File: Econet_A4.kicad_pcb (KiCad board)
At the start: 4 copper layers, 121 x 59.6 mm, 57 parts, among them IC1 SP485REN-L, IC2 74LS123, IC3 LM319M, IC4 LM319M, IC5 68B54, IC6 74AHCT132, IC7 74HCT244, IC8 74HCT245, Q1 AO3401A

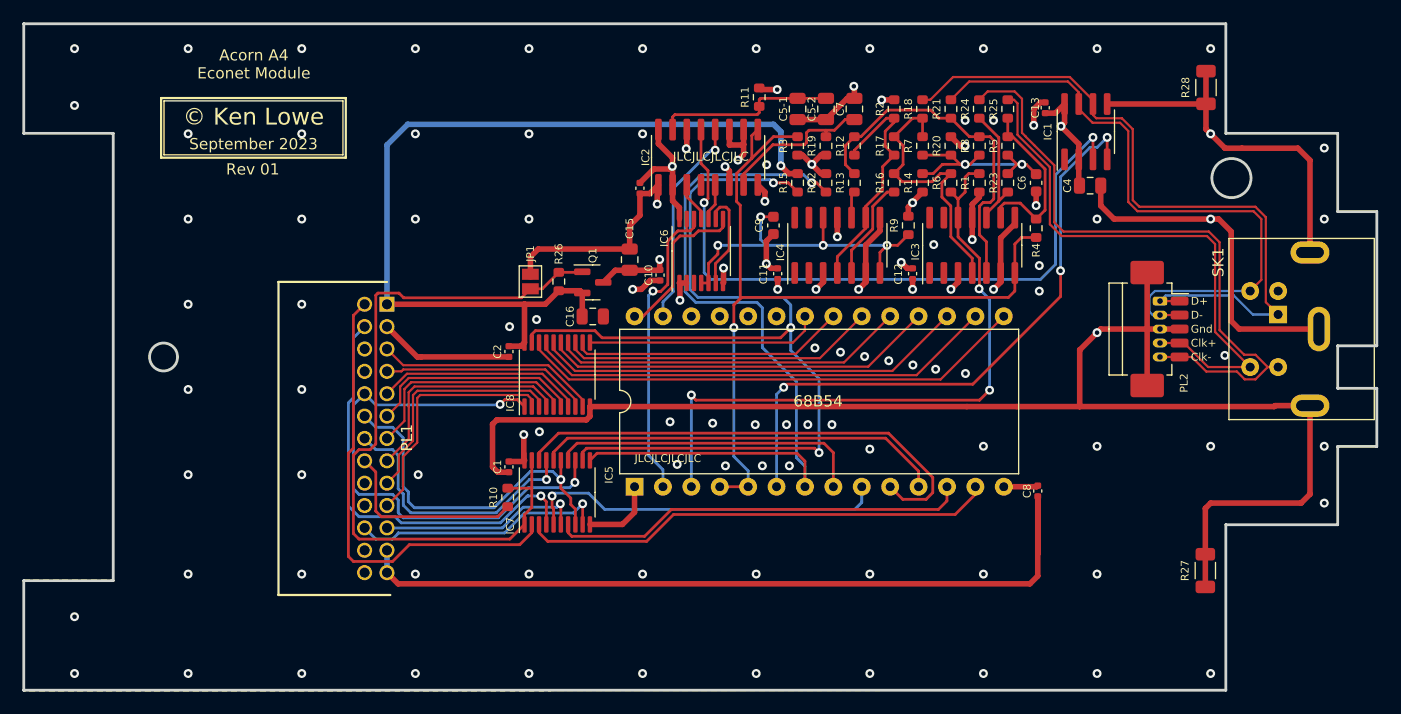
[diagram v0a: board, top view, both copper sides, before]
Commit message: Correct IC 8 data direction
Corrected IC8 data direction
Added activity LEDs
Changed IC7 from 244 to 245
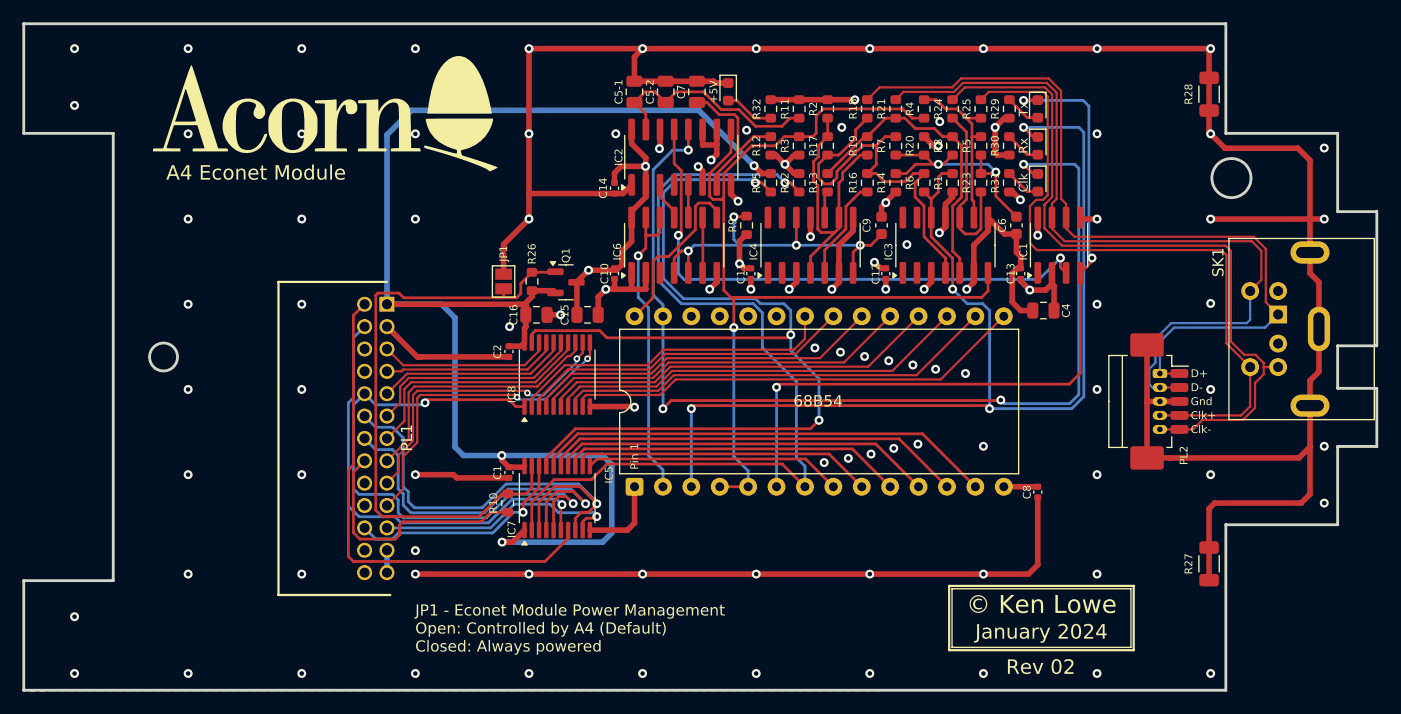
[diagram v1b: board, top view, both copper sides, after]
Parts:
- added G1: LOGO, Econet_A4:AcornLogo2, F.Cu at (132.4, 86.2)
- added LED1: Red, LED_SMD:LED_0603_1608Metric, F.Cu at (195.7, 85.6)
- added LED2: Green, LED_SMD:LED_0603_1608Metric, F.Cu at (195.7, 88.9)
- added LED3: Blue, LED_SMD:LED_0603_1608Metric, F.Cu at (195.7, 92.2)
- added LED4: Green, LED_SMD:LED_0603_1608Metric, F.Cu at (168.0, 84.0)
- added R29: 470R, Resistor_SMD:R_0603_1608Metric, F.Cu at (193.1, 85.6)
- added R30: 1K0, Resistor_SMD:R_0603_1608Metric, F.Cu at (193.1, 88.9)
- added R31: 220R, Resistor_SMD:R_0603_1608Metric, F.Cu at (193.1, 92.2)
- added R32: 2K2, Resistor_SMD:R_0603_1608Metric, F.Cu at (171.8, 85.6)
- IC6: footprint Package_SO:TSSOP-14_4.4x5mm_P0.65mm -> Package_SO:SOIC-14_3.9x8.7mm_P1.27mm
- IC7: value 74HCT244 -> 74HCT245
- PL2: value Conn_01x07 -> Conn_01x06
- SK1: footprint Econet_A4:Connector_Mini-DIN_Female_5Pin_2rows -> Econet_A4:Connector_Mini-DIN_Female_6Pin_2rows
- moved C13 15.0 mm to (194.1, 100.3)
- moved C5-1 14.7 mm to (159.6, 84.0), turned to 90 degrees
- moved R4 14.6 mm to (185.5, 85.6)
- moved R9 14.5 mm to (169.6, 96.0), turned to 90 degrees
- moved C5-2 14.4 mm to (162.4, 84.0), turned to 90 degrees
- moved C7 14.2 mm to (165.2, 84.0)
- moved C4 11.9 mm to (196.2, 103.6), turned to 180 degrees
- moved IC1 10.4 mm to (197.6, 97.8)
- moved C9 9.67 mm to (181.7, 96.0), turned to -90 degrees
- moved PL2 6.48 mm to (205.9, 111.7)
- moved C15 6.21 mm to (155.4, 104.0), turned to 0 degrees
- moved R17 5.95 mm to (176.9, 88.9), turned to 90 degrees
- moved R2 5.95 mm to (176.9, 85.6)
- moved C16 5.04 mm to (150.8, 104.0)
- moved R12 4.94 mm to (171.8, 88.9)
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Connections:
- net Net-(IC1-DI) renamed /Tx_Data
- net Net-(IC2B-~{Q}) renamed /Econet_Clk
- net Net-(IC5-Rx_Data) renamed /Rx_Data
- C5-1 pad 1: Net-(IC2A-RCext) -> GND
- C5-2 pad 1: Net-(IC2A-RCext) -> GND
- IC2 pad 15: Net-(IC2A-RCext) -> GND
- IC7 pad 1: /ECON -> +5V
- IC7 pad 11: /ADLC_nIRQ -> /ADLC_nRST
- IC7 pad 12: /IC8_nCE -> /ADLC_nCS
- IC7 pad 13: /A4_WBE -> /ADLC_A0
- IC7 pad 14: /ADLC_nRST -> /ADLC_A1
- IC7 pad 15: /A4_S2 -> /ADLC_RnW
- IC7 pad 16: /ADLC_A1 -> /ADLC_Clock
- IC7 pad 17: /A4_CLK2 -> /IC8_nCE
- IC7 pad 18: /ADLC_A0 -> /A4_EFIQ
- IC7 pad 2: /A4_LA2 -> /ADLC_nIRQ
- IC7 pad 3: /ADLC_Clock -> /A4_S2
- IC7 pad 4: /A4_LA3 -> /A4_CLK2
- IC7 pad 5: /ADLC_nCS -> /A4_WBE
- IC7 pad 6: /A4_nRST -> /A4_LA3
- IC7 pad 7: /ADLC_RnW -> /A4_LA2
- IC7 pad 9: /A4_EFIQ -> /A4_nRST
- IC8 pad 11: /ADLC_D0 -> /A4_D7
- IC8 pad 12: /ADLC_D1 -> /A4_D6
- IC8 pad 13: /ADLC_D2 -> /A4_D5
- IC8 pad 14: /ADLC_D3 -> /A4_D4
- IC8 pad 15: /ADLC_D4 -> /A4_D3
- IC8 pad 16: /ADLC_D5 -> /A4_D2
- IC8 pad 17: /ADLC_D6 -> /A4_D1
- IC8 pad 18: /ADLC_D7 -> /A4_D0
- IC8 pad 2: /A4_D7 -> /ADLC_D0
- IC8 pad 3: /A4_D6 -> /ADLC_D1
- IC8 pad 4: /A4_D5 -> /ADLC_D2
- IC8 pad 5: /A4_D4 -> /ADLC_D3
- IC8 pad 6: /A4_D3 -> /ADLC_D4
- IC8 pad 7: /A4_D2 -> /ADLC_D5
- IC8 pad 8: /A4_D1 -> /ADLC_D6
- IC8 pad 9: /A4_D0 -> /ADLC_D7
- R11 pad 1: Net-(IC2A-RCext) -> GND
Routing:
- net /Econet_Clk: track 18.8 -> 92.4 mm, vias 1 -> 4
- net /Rx_Data: track 58.3 -> 99.8 mm, vias 3 -> 4
- net /Econpow: track 196.9 -> 218.7 mm, vias 12 -> 14
- net +5V: track 107.5 -> 128.0 mm, vias 2 -> 3
- net Net-(IC2A-RCext): track 16.2 -> 0.00 mm
- net Net-(IC2B-A): track 72.2 -> 86.1 mm
- net /ADLC_A0: track 44.1 -> 30.6 mm
- net /Tx_Data: track 55.6 -> 68.3 mm
- net GND: track 638.5 -> 650.7 mm, vias 105 -> 96
- net /Data-: track 57.9 -> 70.1 mm
- net /Clk+: track 49.8 -> 61.4 mm
- net /ECON: track 66.6 -> 55.0 mm
- net Net-(IC3A-+): track 24.9 -> 35.8 mm
- net /Data_En: track 60.1 -> 50.0 mm
- net /A4_S2: track 31.9 -> 41.4 mm
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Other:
- board text added: "+5V"
- board text added: "A4 Econet Module"
- board text added: "Clk"
- board text added: "JP1 - Econet Module Power Management Open: Controlled by A4 (Default) Closed: Always powered"
- board text added: "January 2024"
- board text added: "Pin 1"
- board text added: "Rev 02"
- board text added: "Rx"
- board text added: "Tx"
- board text removed: "Acorn A4 Econet Module"
- board text removed: "JLCJLCJLCJLC"
- board text removed: "Rev 01"
- board text removed: "September 2023"
